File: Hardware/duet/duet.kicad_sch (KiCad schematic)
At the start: 0 parts

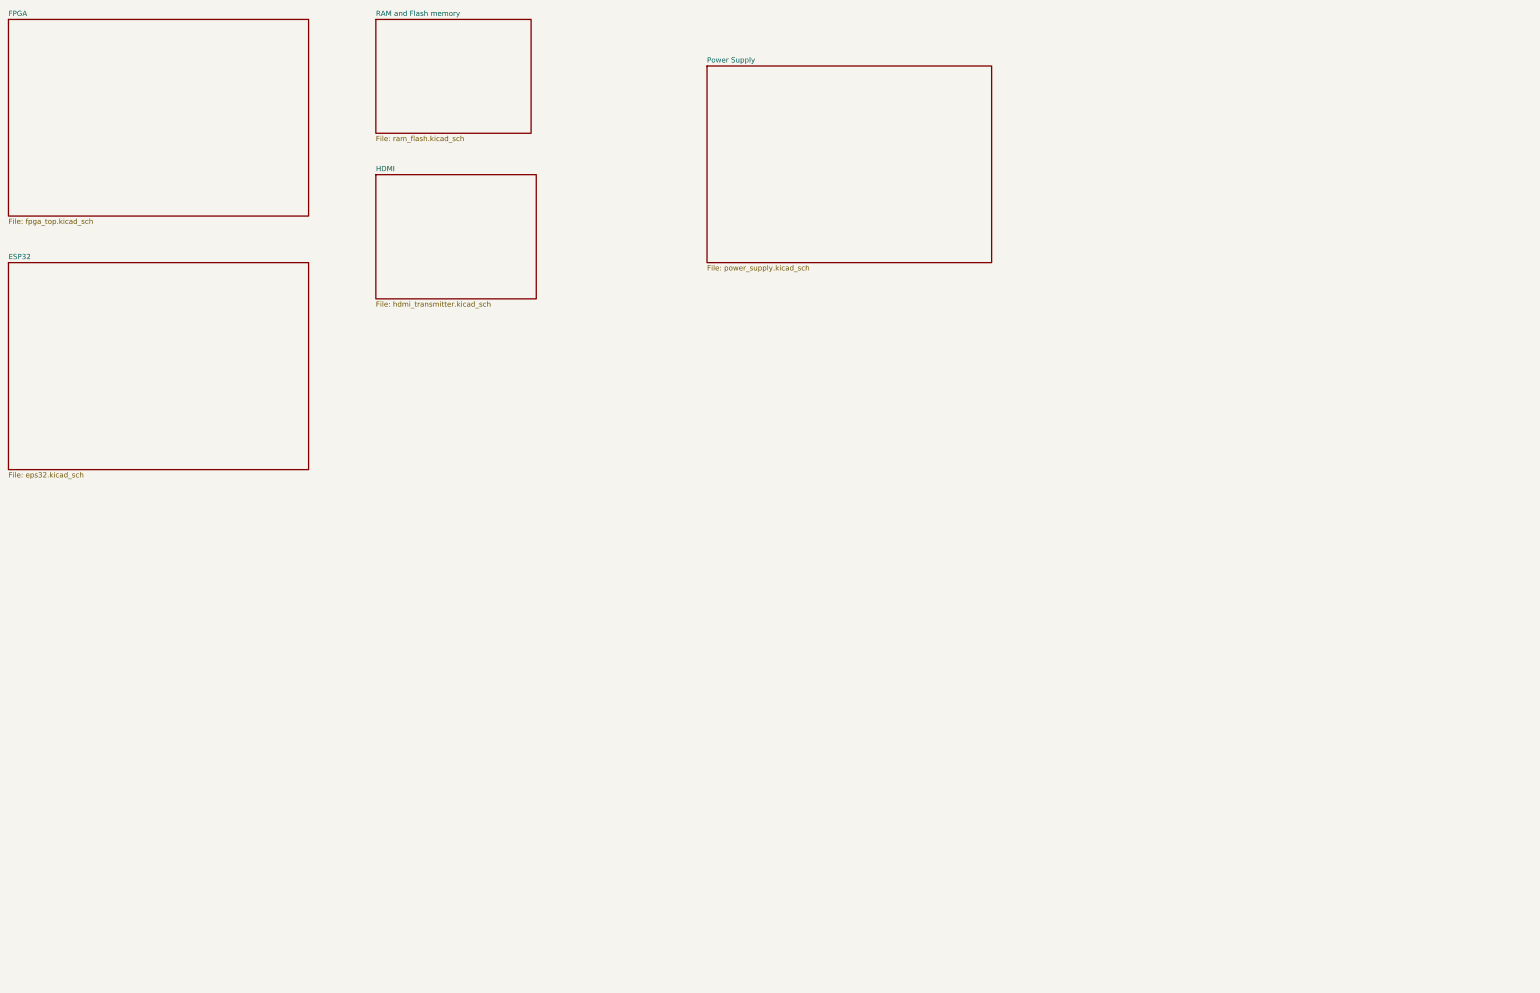
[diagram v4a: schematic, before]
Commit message: Add mezzanine connector and finalze HDMI
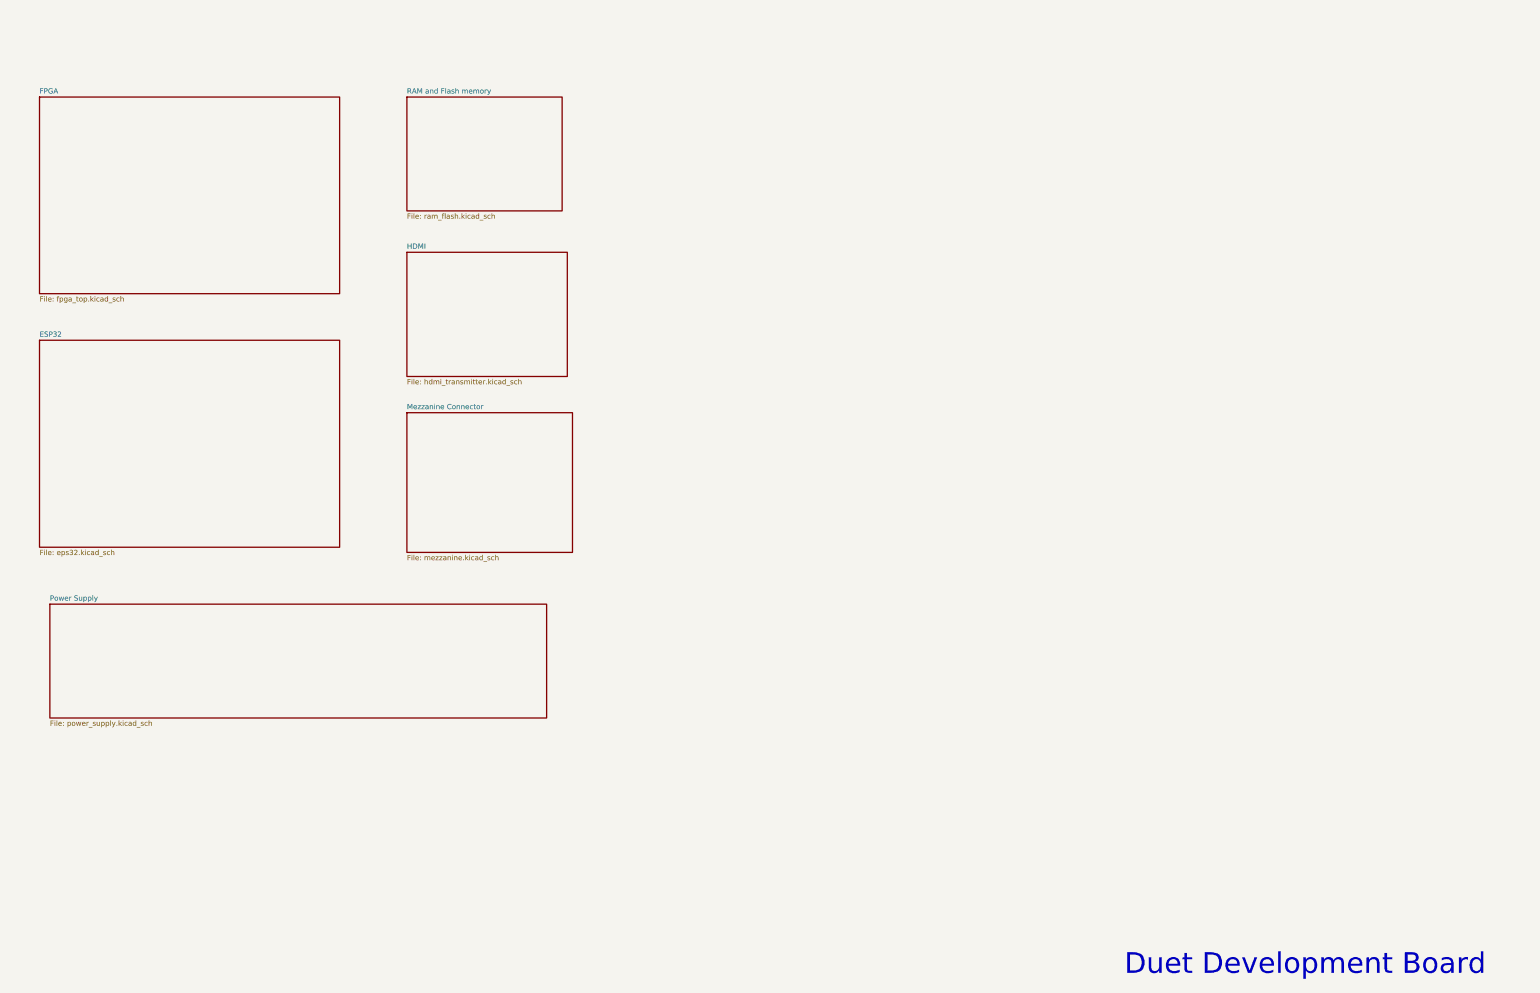
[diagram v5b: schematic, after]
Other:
- added sheet Mezzanine Connector (mezzanine.kicad_sch)
- note added: "Duet Development Board"
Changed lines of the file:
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@@
 	(generator_version "10.0")
 	(paper "A3")
-	(sheet
-		(at 34.29 29.21)
+	(text "Duet Development Board"
+		(exclude_from_sim no)
+		(at 352.552 261.112 0)
+		(effects
+			(font
+				(size 5.08 5.08)
+			)
+		)
+	)
+	(sheet
+		(at 132.08 125.73)
+		(size 40.64 34.29)
+		(exclude_from_sim no)
+		(in_bom yes)
+		(on_board yes)
+		(dnp no)
+		(fields_autoplaced yes)
+		(stroke
+			(width 0.1524)
+			(type solid)
+		)
+		(fill
+			(color 0 0 0 0)
+		)
+		(property "Sheetname" "Mezzanine Connector"
+			(at 132.08 125.0184 0)
+			(show_name no)
+			(do_not_autoplace no)
+			(effects
+				(font
+					(size 1.27 1.27)
+				)
+				(justify left bottom)
+			)
+		)
+		(property "Sheetfile" "mezzanine.kicad_sch"
+			(at 132.08 160.6046 0)
+			(show_name no)
+			(do_not_autoplace no)
+			(effects
+				(font
+					(size 1.27 1.27)
+				)
+				(justify left top)
+			)
+		)
+		(instances
+			(project "duet"
+				(path "/0eef67e7-bb51-4885-9085-a6db10d7906a"
+					(page "7")
+				)
+			)
+		)
+	)
+	(sheet
+		(at 41.91 48.26)
 		(size 73.66 48.26)
 		(exclude_from_sim no)
@@
 		)
 		(property "Sheetname" "FPGA"
-			(at 34.29 28.4984 0)
+			(at 41.91 47.5484 0)
 			(show_name no)
 			(do_not_autoplace no)
@@
 		)
 		(property "Sheetfile" "fpga_top.kicad_sch"
-			(at 34.29 78.0546 0)
+			(at 41.91 97.1046 0)
 			(show_name no)
 			(do_not_autoplace no)
@@
 	)
 	(sheet
-		(at 34.29 88.9)
+		(at 41.91 107.95)
 		(size 73.66 50.8)
 		(exclude_from_sim no)
@@
 		)
 		(property "Sheetname" "ESP32"
-			(at 34.29 88.1884 0)
+			(at 41.91 107.2384 0)
 			(show_name no)
 			(do_not_autoplace no)
@@
 		)
 		(property "Sheetfile" "eps32.kicad_sch"
-			(at 34.29 140.2846 0)
+			(at 41.91 159.3346 0)
 			(show_name no)
 			(do_not_autoplace no)
@@
 	)
 	(sheet
-		(at 205.74 40.64)
-		(size 69.85 48.26)
+		(at 44.45 172.72)
+		(size 121.92 27.94)
 		(exclude_from_sim no)
 		(in_bom yes)
@@
 		)
 		(property "Sheetname" "Power Supply"
-			(at 205.74 39.9284 0)
+			(at 44.45 172.0084 0)
 			(show_name no)
 			(do_not_autoplace no)
@@
 		)
 		(property "Sheetfile" "power_supply.kicad_sch"
-			(at 205.74 89.4846 0)
+			(at 44.45 201.2446 0)
 			(show_name no)
 			(do_not_autoplace no)
@@
 	)
 	(sheet
-		(at 124.46 29.21)
+		(at 132.08 48.26)
 		(size 38.1 27.94)
 		(exclude_from_sim no)
@@
 		)
 		(property "Sheetname" "RAM and Flash memory"
-			(at 124.46 28.4984 0)
+			(at 132.08 47.5484 0)
 			(show_name no)
 			(do_not_autoplace no)
@@
 		)
 		(property "Sheetfile" "ram_flash.kicad_sch"
-			(at 124.46 57.7346 0)
+			(at 132.08 76.7846 0)
 			(show_name no)
 			(do_not_autoplace no)
@@
 	)
 	(sheet
-		(at 124.46 67.31)
+		(at 132.08 86.36)
 		(size 39.37 30.48)
 		(exclude_from_sim no)
@@
 		)
 		(property "Sheetname" "HDMI"
-			(at 124.46 66.5984 0)
+			(at 132.08 85.6484 0)
 			(show_name no)
 			(do_not_autoplace no)
@@
 		)
 		(property "Sheetfile" "hdmi_transmitter.kicad_sch"
-			(at 124.46 98.3746 0)
-			(show_name no)
-			(do_not_autoplace no)
+			(at 132.08 117.4246 0)
+			(show_name no)
+			(do_not_autoplace no)
